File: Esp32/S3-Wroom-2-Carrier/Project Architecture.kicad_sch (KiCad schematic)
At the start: 0 parts

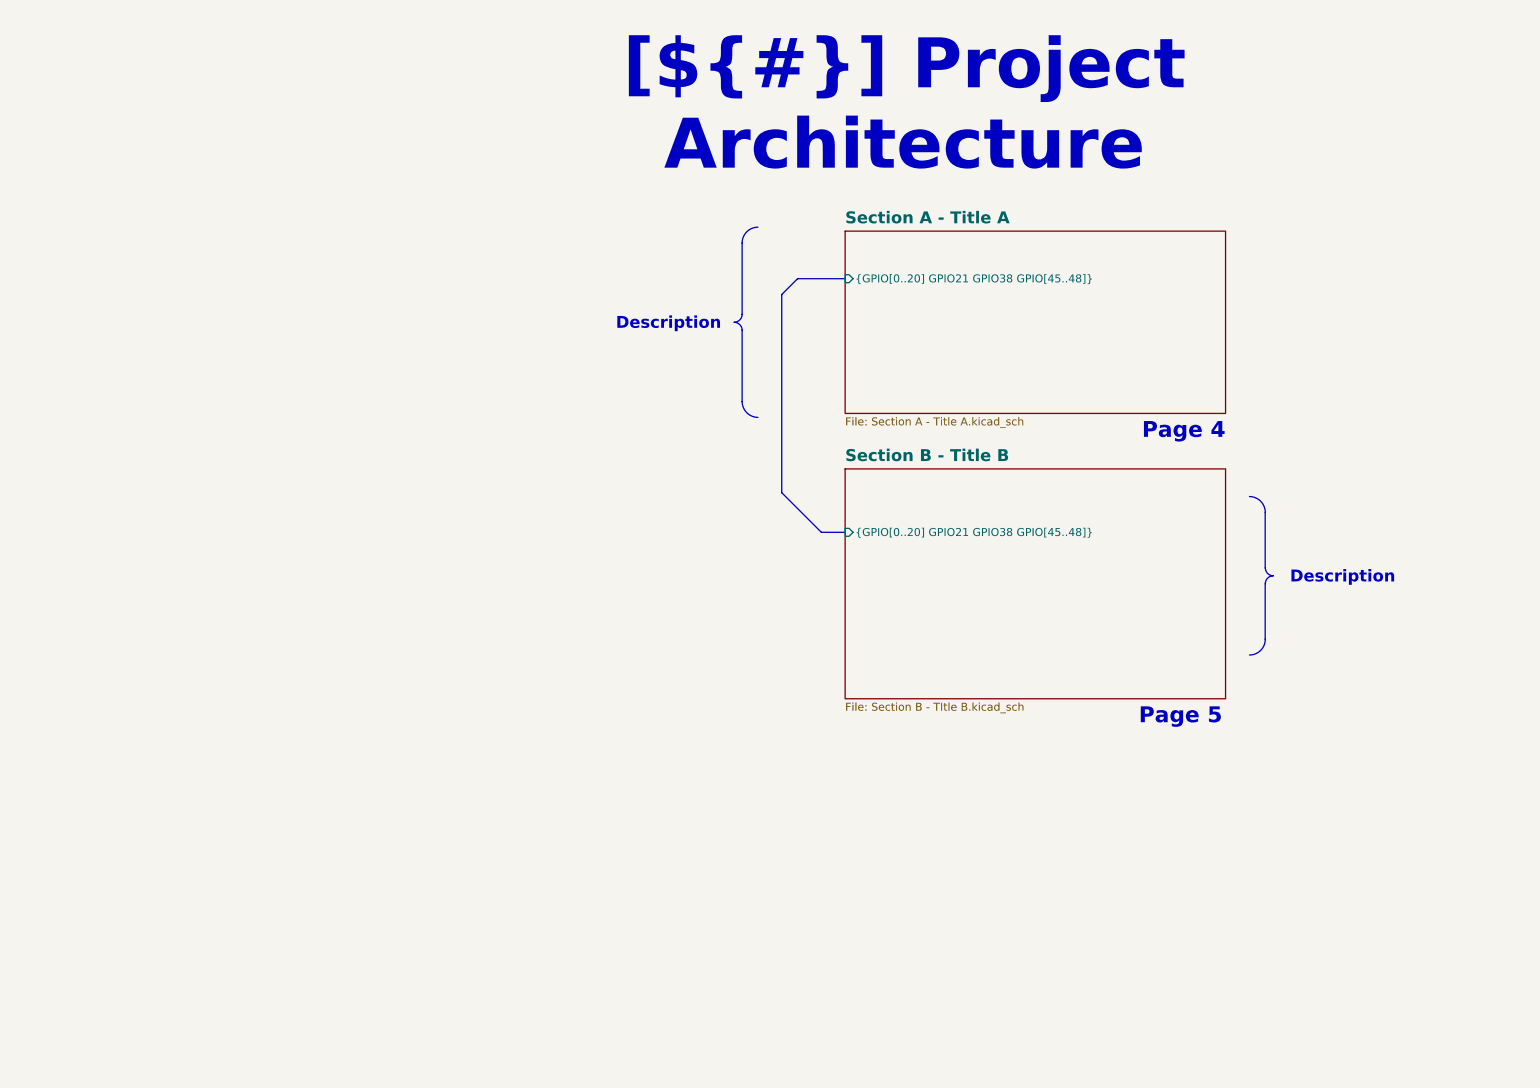
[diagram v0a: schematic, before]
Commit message: Power sheet
Added Esp32 power sheet and rename previous sheets
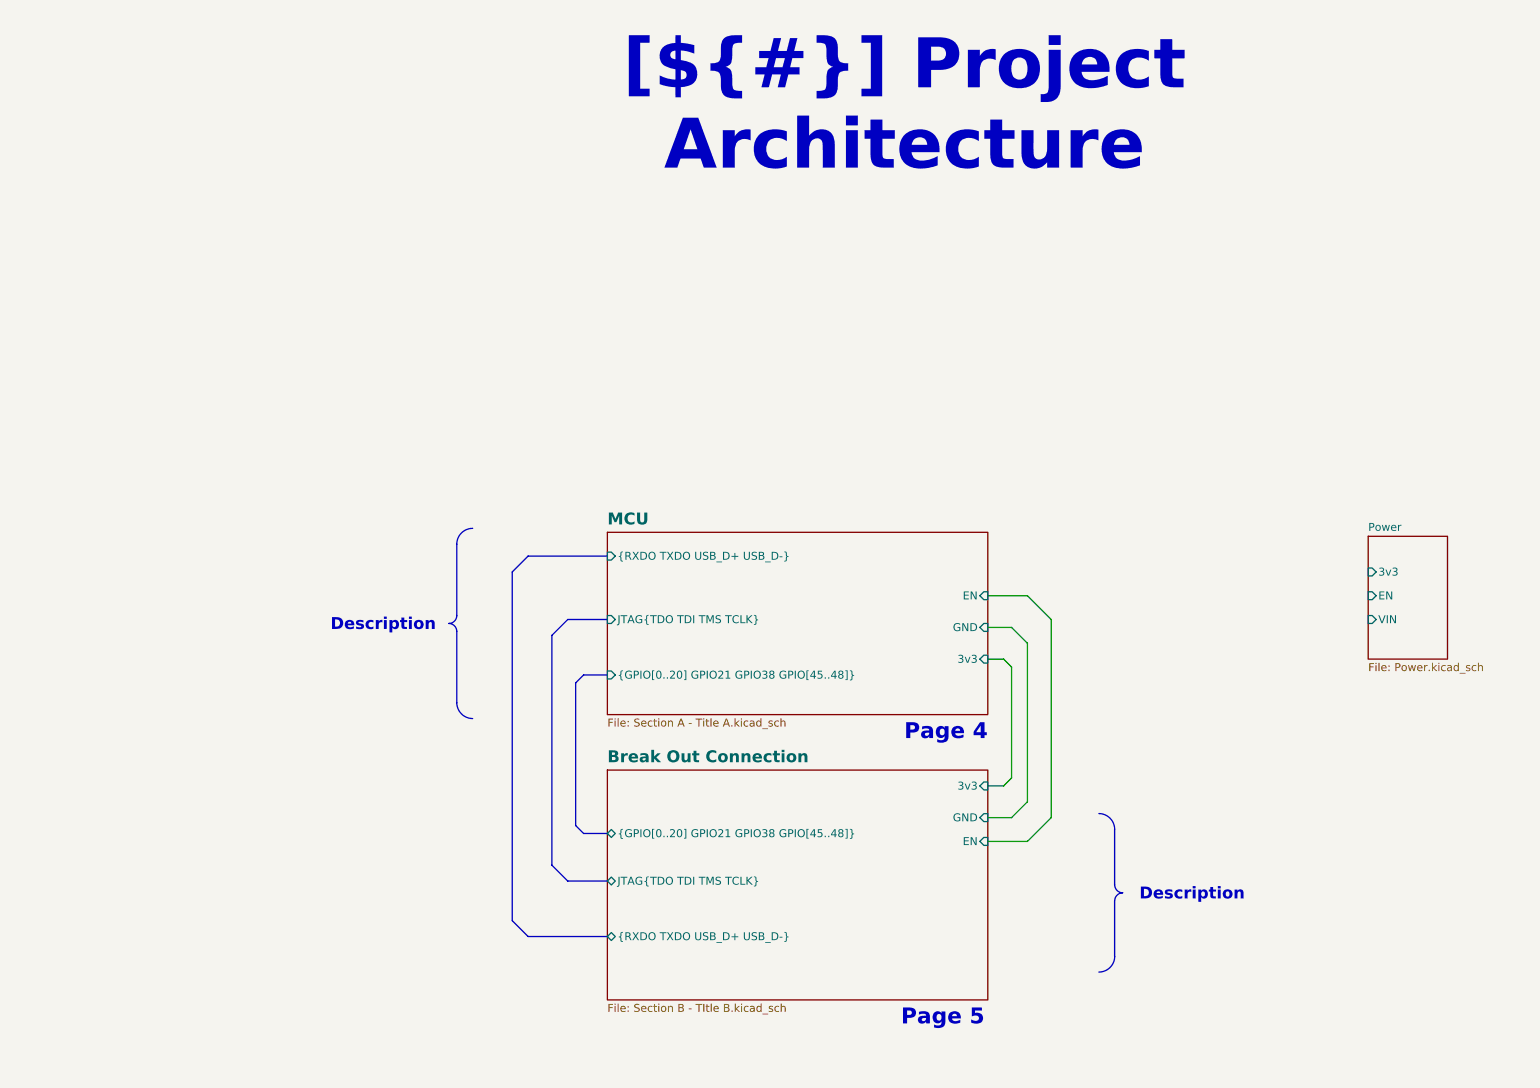
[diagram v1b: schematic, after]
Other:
- sheet Section A - Title A renamed MCU
- sheet Section B - Title B renamed Break Out Connection
- added sheet Power (Power.kicad_sch)
- sheet Break Out Connection ports: added 3v3, EN, GND, JTAG{TDO TDI TMS TCLK}, {RXDO TXDO USB_D+ USB_D-}; removed none
- sheet MCU ports: added 3v3, EN, GND, JTAG{TDO TDI TMS TCLK}, {RXDO TXDO USB_D+ USB_D-}; removed none

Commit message: Connectors
Lower connector routed
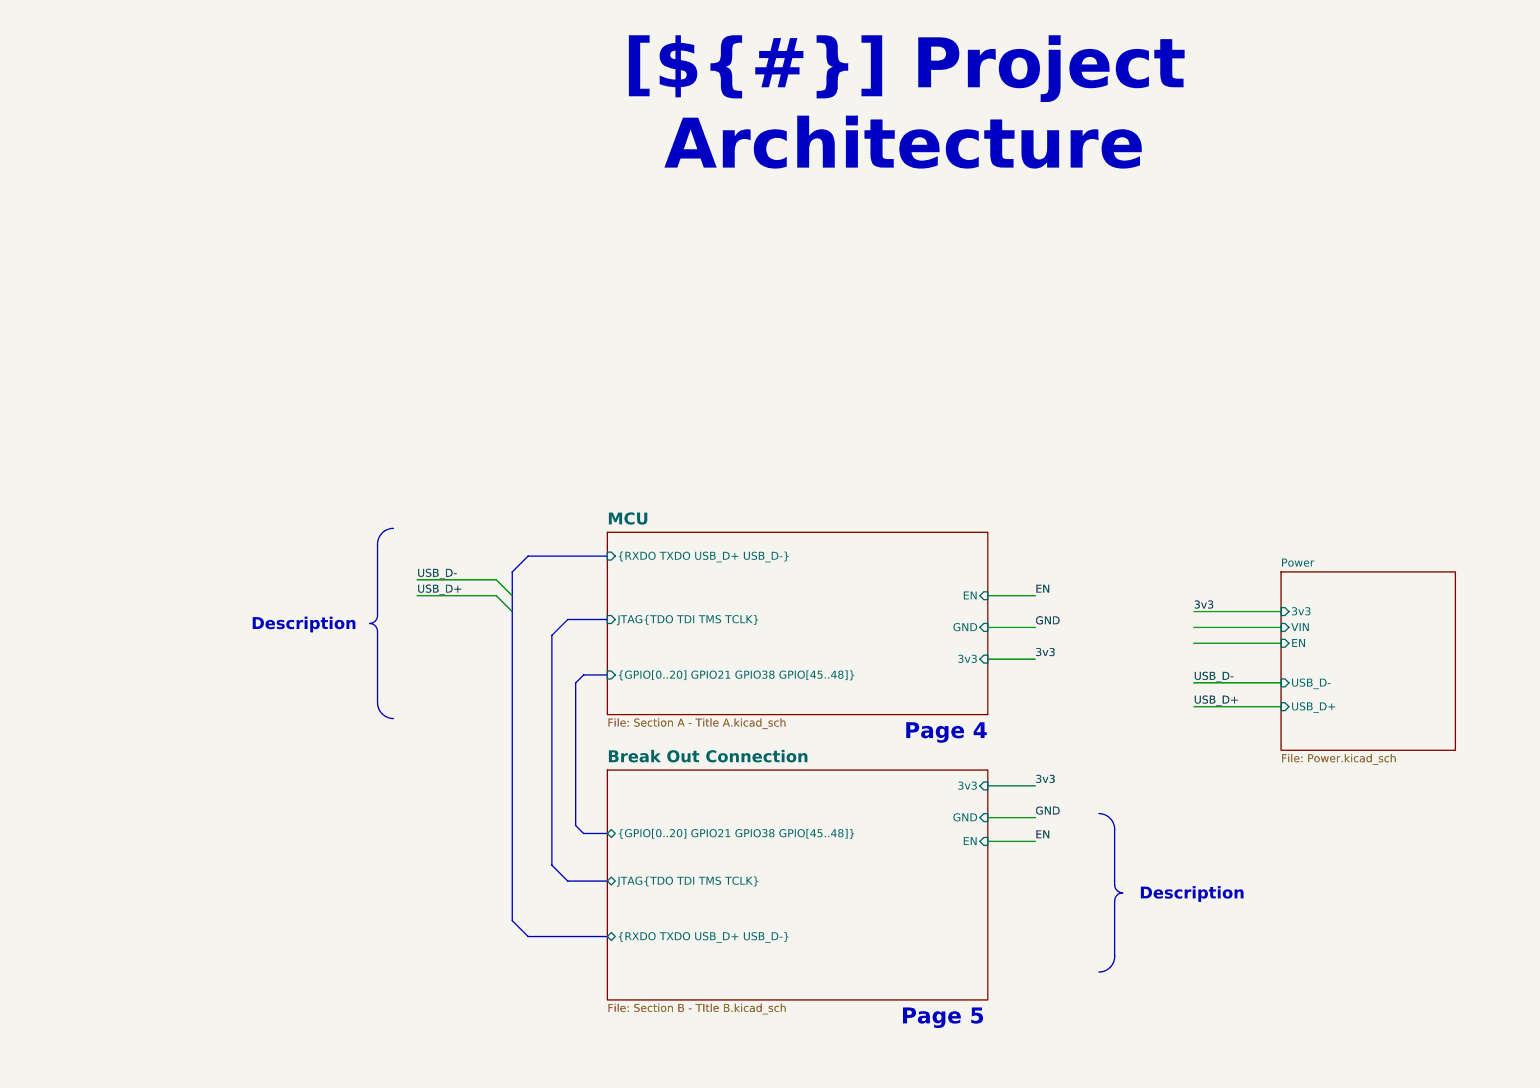
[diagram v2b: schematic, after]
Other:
- sheet Power ports: added USB_D+, USB_D-; removed none
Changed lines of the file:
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@@
 	)
 	(arc
-		(start 138.43 108.585)
-		(mid 138.0551 109.4801)
-		(end 137.16 109.855)
+		(start 125.73 108.585)
+		(mid 125.3551 109.4801)
+		(end 124.46 109.855)
 		(stroke
 			(width 0)
@@
 	)
 	(arc
-		(start 137.16 109.855)
-		(mid 138.0551 110.2299)
-		(end 138.43 111.125)
+		(start 124.46 109.855)
+		(mid 125.3551 110.2299)
+		(end 125.73 111.125)
 		(stroke
 			(width 0)
@@
 	)
 	(arc
-		(start 138.43 97.155)
-		(mid 139.1739 95.3589)
-		(end 140.97 94.615)
+		(start 125.73 97.155)
+		(mid 126.4739 95.3589)
+		(end 128.27 94.615)
 		(stroke
 			(width 0)
@@
 	)
 	(arc
-		(start 140.97 125.095)
-		(mid 139.1798 124.3452)
-		(end 138.43 122.555)
+		(start 128.27 125.095)
+		(mid 126.4798 124.3452)
+		(end 125.73 122.555)
 		(stroke
 			(width 0)
@@
 	(text_box "Description"
 		(exclude_from_sim no)
-		(at 119.38 107.315 0)
+		(at 106.68 107.315 0)
 		(size 17.145 5.08)
 		(margins 1.4287 1.4287 1.4287 1.4287)
@@
 		)
 	)
-	(wire
-		(pts
-			(xy 233.68 140.97) (xy 229.87 144.78)
+	(bus_entry
+		(at 147.32 107.95)
+		(size -2.54 -2.54)
+		(stroke
+			(width 0)
+			(type default)
+		)
+	)
+	(bus_entry
+		(at 147.32 105.41)
+		(size -2.54 -2.54)
+		(stroke
+			(width 0)
+			(type default)
+		)
+	)
+	(wire
+		(pts
+			(xy 256.54 110.49) (xy 270.51 110.49)
 		)
 		(stroke
@@
 	(polyline
 		(pts
-			(xy 138.43 111.125) (xy 138.43 122.555)
-		)
-		(stroke
-			(width 0)
-			(type default)
-		)
-	)
-	(wire
-		(pts
-			(xy 229.87 138.43) (xy 227.33 140.97)
+			(xy 125.73 111.125) (xy 125.73 122.555)
+		)
+		(stroke
+			(width 0)
+			(type default)
+		)
+	)
+	(wire
+		(pts
+			(xy 256.54 119.38) (xy 270.51 119.38)
 		)
 		(stroke
@@
 		)
 	)
-	(wire
-		(pts
-			(xy 226.06 115.57) (xy 227.33 116.84)
+	(bus
+		(pts
+			(xy 147.32 107.95) (xy 147.32 157.48)
+		)
+		(stroke
+			(width 0)
+			(type default)
+		)
+	)
+	(wire
+		(pts
+			(xy 256.54 123.19) (xy 270.51 123.19)
 		)
 		(stroke
@@
 	(wire
 		(pts
-			(xy 223.52 105.41) (xy 229.87 105.41)
-		)
-		(stroke
-			(width 0)
-			(type default)
-		)
-	)
-	(wire
-		(pts
-			(xy 223.52 115.57) (xy 226.06 115.57)
+			(xy 223.52 105.41) (xy 231.14 105.41)
+		)
+		(stroke
+			(width 0)
+			(type default)
+		)
+	)
+	(wire
+		(pts
+			(xy 223.52 115.57) (xy 231.14 115.57)
 		)
 		(stroke
@@
 	(polyline
 		(pts
-			(xy 138.43 108.585) (xy 138.43 97.155)
-		)
-		(stroke
-			(width 0)
-			(type default)
-		)
-	)
-	(wire
-		(pts
-			(xy 233.68 109.22) (xy 233.68 140.97)
-		)
-		(stroke
-			(width 0)
-			(type default)
-		)
-	)
-	(wire
-		(pts
-			(xy 227.33 110.49) (xy 229.87 113.03)
+			(xy 125.73 108.585) (xy 125.73 97.155)
 		)
 		(stroke
@@
 	(wire
 		(pts
-			(xy 223.52 140.97) (xy 227.33 140.97)
-		)
-		(stroke
-			(width 0)
-			(type default)
-		)
-	)
-	(wire
-		(pts
-			(xy 227.33 116.84) (xy 227.33 134.62)
-		)
-		(stroke
-			(width 0)
-			(type default)
-		)
-	)
-	(wire
-		(pts
-			(xy 223.52 110.49) (xy 227.33 110.49)
+			(xy 223.52 140.97) (xy 231.14 140.97)
+		)
+		(stroke
+			(width 0)
+			(type default)
+		)
+	)
+	(bus
+		(pts
+			(xy 147.32 105.41) (xy 147.32 107.95)
+		)
+		(stroke
+			(width 0)
+			(type default)
+		)
+	)
+	(wire
+		(pts
+			(xy 223.52 110.49) (xy 231.14 110.49)
 		)
 		(stroke
@@
 	(wire
 		(pts
-			(xy 223.52 144.78) (xy 229.87 144.78)
+			(xy 223.52 144.78) (xy 231.14 144.78)
+		)
+		(stroke
+			(width 0)
+			(type default)
+		)
+	)
+	(wire
+		(pts
+			(xy 256.54 113.03) (xy 270.51 113.03)
 		)
 		(stroke
@@
 		)
 	)
+	(wire
+		(pts
+			(xy 132.08 105.41) (xy 144.78 105.41)
+		)
+		(stroke
+			(width 0)
+			(type default)
+		)
+	)
 	(bus
 		(pts
@@
 	(wire
 		(pts
-			(xy 229.87 113.03) (xy 229.87 138.43)
+			(xy 256.54 107.95) (xy 270.51 107.95)
 		)
 		(stroke
@@
 	(wire
 		(pts
-			(xy 223.52 135.89) (xy 226.06 135.89)
+			(xy 223.52 135.89) (xy 231.14 135.89)
 		)
 		(stroke
@@
 	(wire
 		(pts
-			(xy 229.87 105.41) (xy 233.68 109.22)
-		)
-		(stroke
-			(width 0)
-			(type default)
-		)
-	)
-	(wire
-		(pts
-			(xy 227.33 134.62) (xy 226.06 135.89)
+			(xy 132.08 102.87) (xy 144.78 102.87)
 		)
 		(stroke
@@
 	(bus
 		(pts
-			(xy 147.32 101.6) (xy 147.32 157.48)
-		)
-		(stroke
-			(width 0)
-			(type default)
+			(xy 147.32 101.6) (xy 147.32 105.41)
+		)
+		(stroke
+			(width 0)
+			(type default)
+		)
+	)
+	(label "GND"
+		(at 231.14 110.49 0)
+		(effects
+			(font
+				(size 1.27 1.27)
+			)
+			(justify left bottom)
+		)
+	)
+	(label "USB_D-"
+		(at 132.08 102.87 0)
+		(effects
+			(font
+				(size 1.27 1.27)
+			)
+			(justify left bottom)
+		)
+	)
+	(label "USB_D-"
+		(at 256.54 119.38 0)
+		(effects
+			(font
+				(size 1.27 1.27)
+			)
+			(justify left bottom)
+		)
+	)
+	(label "3v3"
+		(at 256.54 107.95 0)
+		(effects
+			(font
+				(size 1.27 1.27)
+			)
+			(justify left bottom)
+		)
+	)
+	(label "EN"
+		(at 231.14 144.78 0)
+		(effects
+			(font
+				(size 1.27 1.27)
+			)
+			(justify left bottom)
+		)
+	)
+	(label "3v3"
+		(at 231.14 115.57 0)
+		(effects
+			(font
+				(size 1.27 1.27)
+			)
+			(justify left bottom)
+		)
+	)
+	(label "3v3"
+		(at 231.14 135.89 0)
+		(effects
+			(font
+				(size 1.27 1.27)
+			)
+			(justify left bottom)
+		)
+	)
+	(label "USB_D+"
+		(at 132.08 105.41 0)
+		(effects
+			(font
+				(size 1.27 1.27)
+			)
+			(justify left bottom)
+		)
+	)
+	(label "USB_D+"
+		(at 256.54 123.19 0)
+		(effects
+			(font
+				(size 1.27 1.27)
+			)
+			(justify left bottom)
+		)
+	)
+	(label "EN"
+		(at 231.14 105.41 0)
+		(effects
+			(font
+				(size 1.27 1.27)
+			)
+			(justify left bottom)
+		)
+	)
+	(label "GND"
+		(at 231.14 140.97 0)
+		(effects
+			(font
+				(size 1.27 1.27)
+			)
+			(justify left bottom)
 		)
 	)
 	(sheet
-		(at 284.48 95.885)
-		(size 12.7 19.685)
+		(at 270.51 101.6)
+		(size 27.94 28.575)
 		(exclude_from_sim no)
 		(in_bom yes)
@@
 		)
 		(property "Sheetname" "Power"
-			(at 284.48 95.1734 0)
+			(at 270.51 100.8884 0)
 			(effects
 				(font
@@
 		)
 		(property "Sheetfile" "Power.kicad_sch"
-			(at 284.48 116.1546 0)
+			(at 270.51 130.7596 0)
 			(effects
 				(font
@@
 		)
 		(pin "3v3" input
-			(at 284.48 101.6 180)
+			(at 270.51 107.95 180)
 			(effects
 				(font
@@
 		)
 		(pin "EN" input
-			(at 284.48 105.41 180)
+			(at 270.51 113.03 180)
 			(effects
 				(font
@@
 		)
 		(pin "VIN" input
-			(at 284.48 109.22 180)
+			(at 270.51 110.49 180)
 			(effects
 				(font
+					(size 1.27 1.27)
+				)
+				(justify left)
+			)
+		)
+		(pin "USB_D-" input
+			(at 270.51 119.38 180)
+			(effects
+				(font
+					(size 1.27 1.27)
+				)
+				(justify left)
+			)
+		)
+		(pin "USB_D+" input
+			(at 270.51 123.19 180)
+			(effects
+				(font

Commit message: Routing
Routing finished needs to be verify
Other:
- sheet Break Out Connection ports: added {GPIO[0..20] GPIO21 GPIO[35..38] GPIO[45..48]}; removed {GPIO[0..20] GPIO21 GPIO38 GPIO[45..48]}
- sheet MCU ports: added {GPIO[0..20] GPIO21 GPIO[35..38] GPIO[45..48]}; removed {GPIO[0..20] GPIO21 GPIO38 GPIO[45..48]}
- note added: "Page 6"
